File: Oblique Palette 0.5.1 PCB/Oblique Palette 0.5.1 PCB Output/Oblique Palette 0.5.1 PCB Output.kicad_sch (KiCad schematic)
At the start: 25 parts

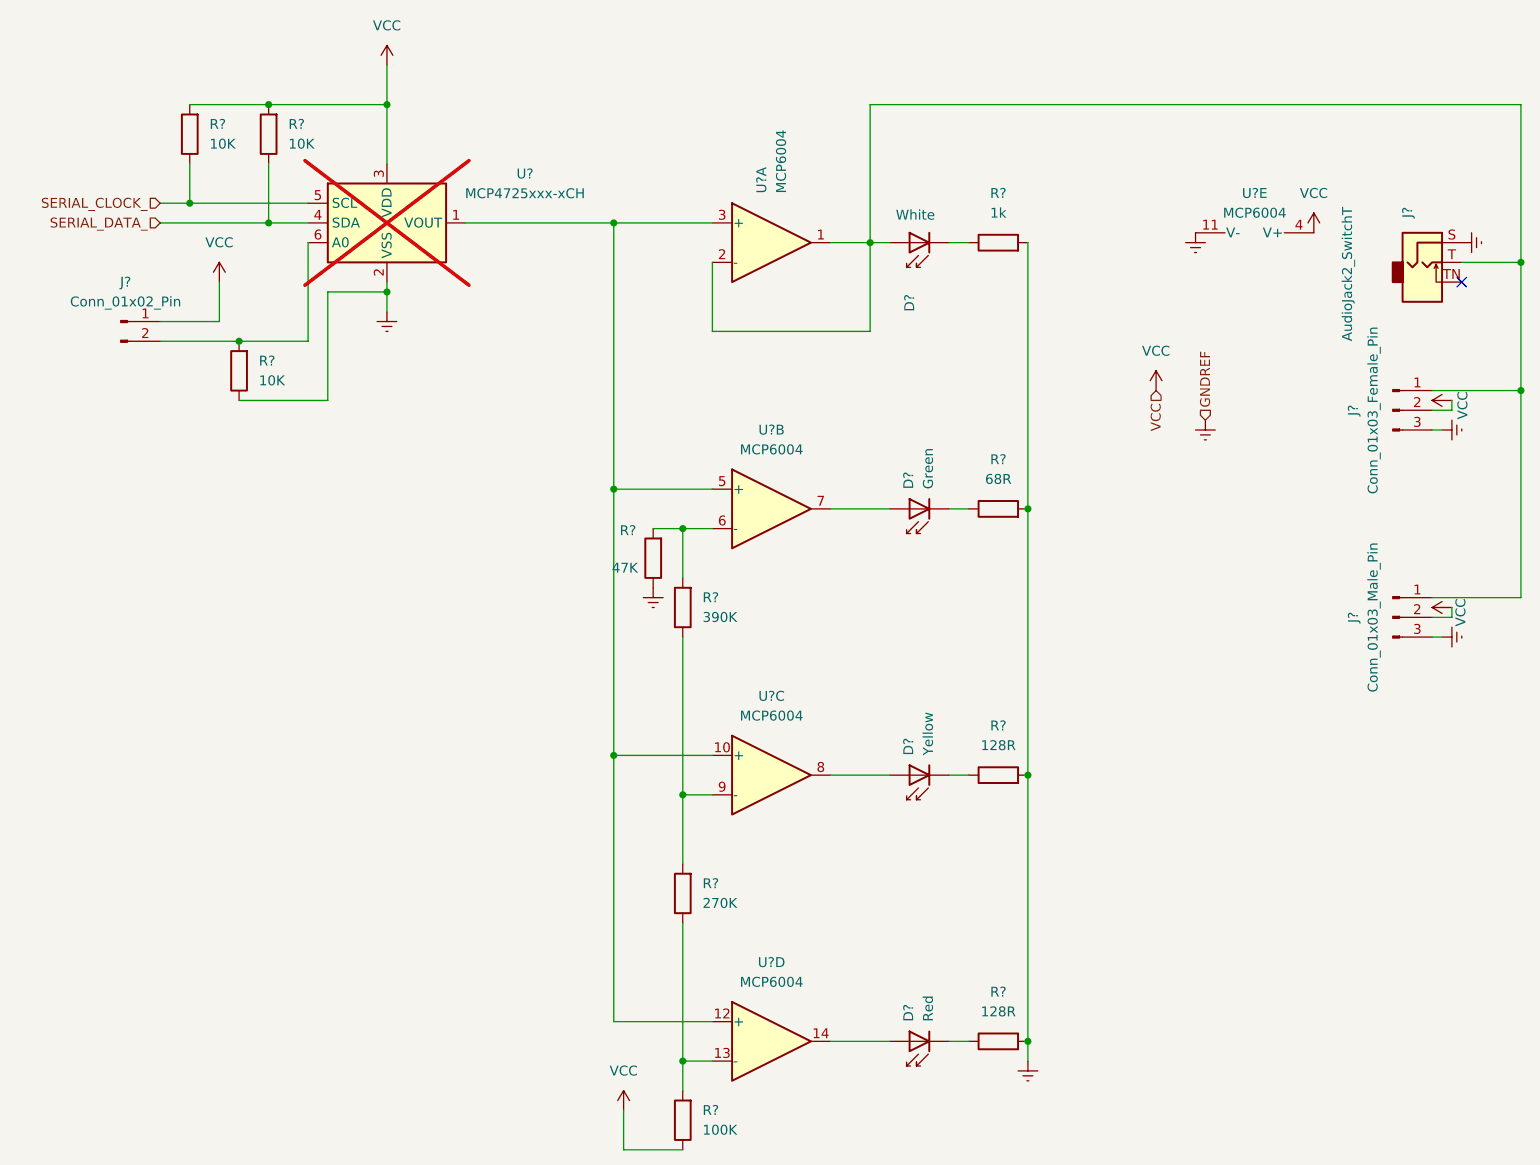
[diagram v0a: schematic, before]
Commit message: PCB corrections for 0.5.3
• Main output LED is now between op amp and feedback loop, so it will brighten at the first whiff of voltage.
• Errant wire between VBus and input potentiometer will allow us to have signals other than 5V
• Servos are now powered by V_SERVO as well as VBus.

TO DO: Differentiate A0 and A1 DACs
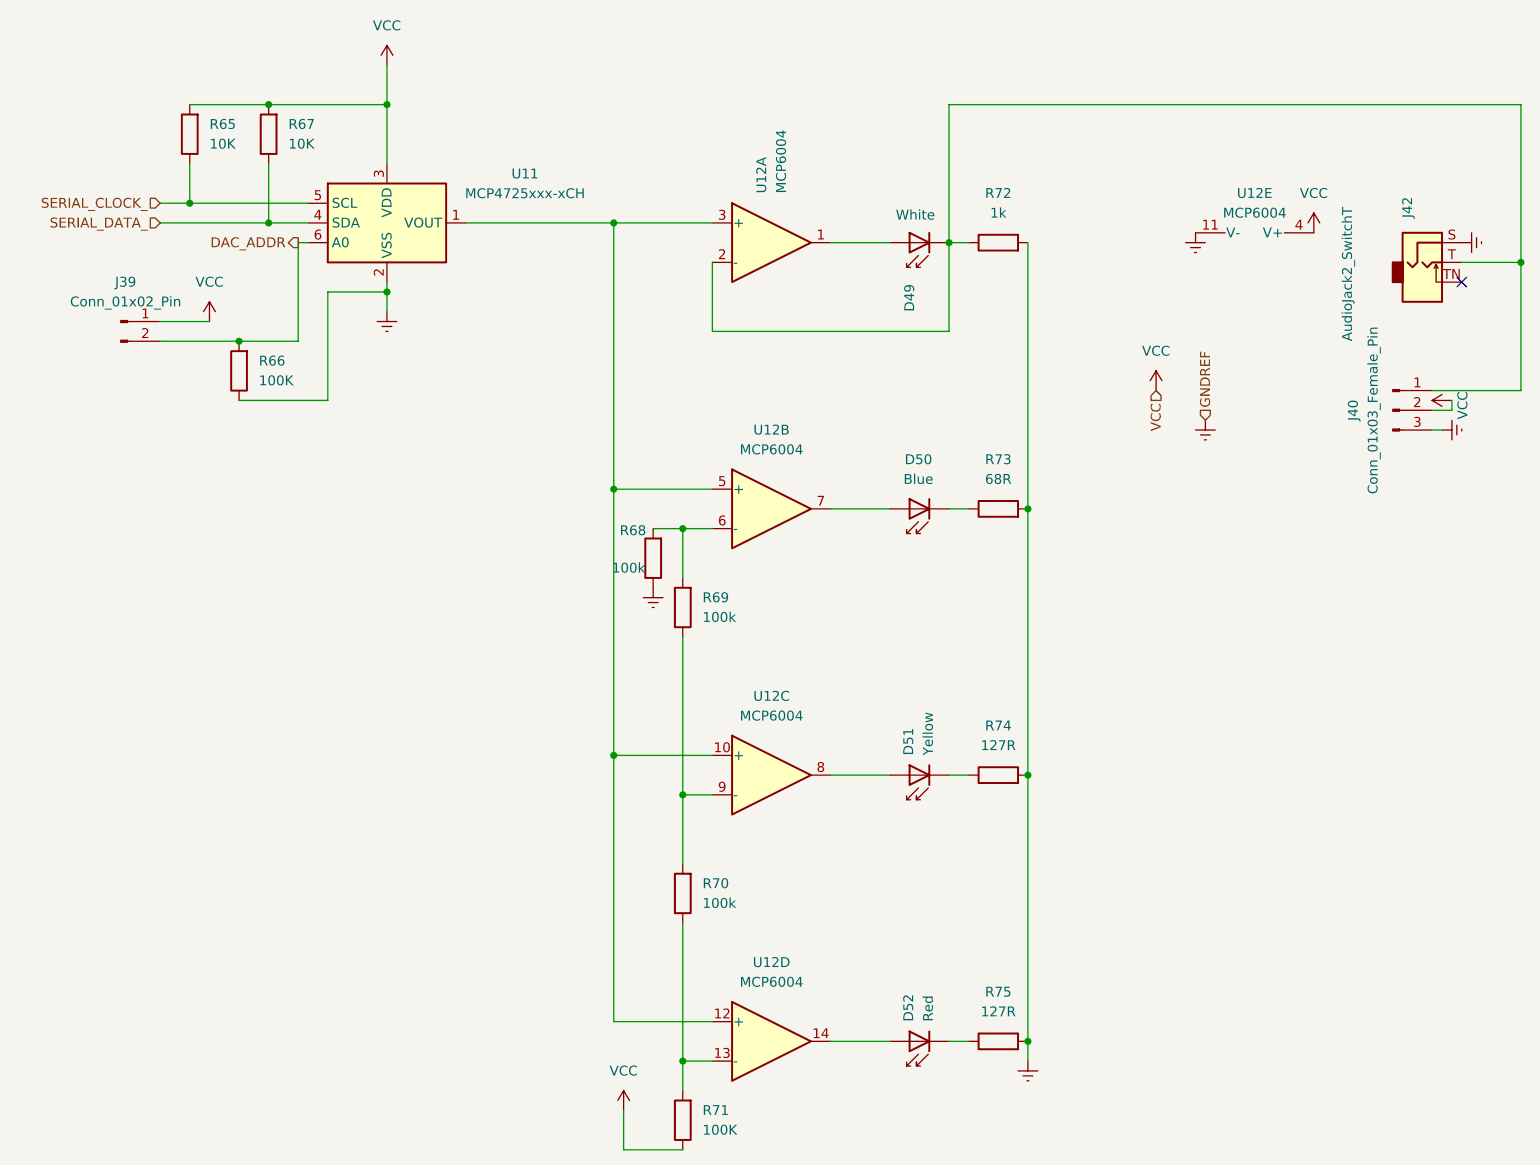
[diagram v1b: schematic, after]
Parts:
- removed J?: Conn_01x03_Male_Pin, Connector_PinHeader_2.54mm:PinHeader_1x03_P2.54mm_Vertical, symbol Connector:Conn_01x03_Pin
- D50: renamed from D?; value Green -> Blue
- R66: renamed from R?; value 10K -> 100K
- R68: renamed from R?; value 47K -> 100k
- R69: renamed from R?; value 390K -> 100k
- R70: renamed from R?; value 270K -> 100k
- R74, R75: renamed from R?; value 128R -> 127R
- U11: renamed from U?; now fitted
- gave numbers to parts that had none: 12
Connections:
- net DAC_ADDR: now reaches J39.2 (Pin_2), R66.2, U11.6 (A0)
- net at J40.1 (Pin_1), J42.T, U12.2 (-): now also D49.1 (K), R72.1; no longer D49.2 (A), U12.1
- new net: D49.2 (A), U12.1

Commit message: Update OUTPUT channels with 3 LEDs and appropriate resistors
Output channels how have RED (>3.6V), YELLOW (<2.7V) and WHITE (<0, increasing in brightness up to 5V) indicator LEDs.

Output op amp now has a 1k resistor to prevent in-use whoopsies.
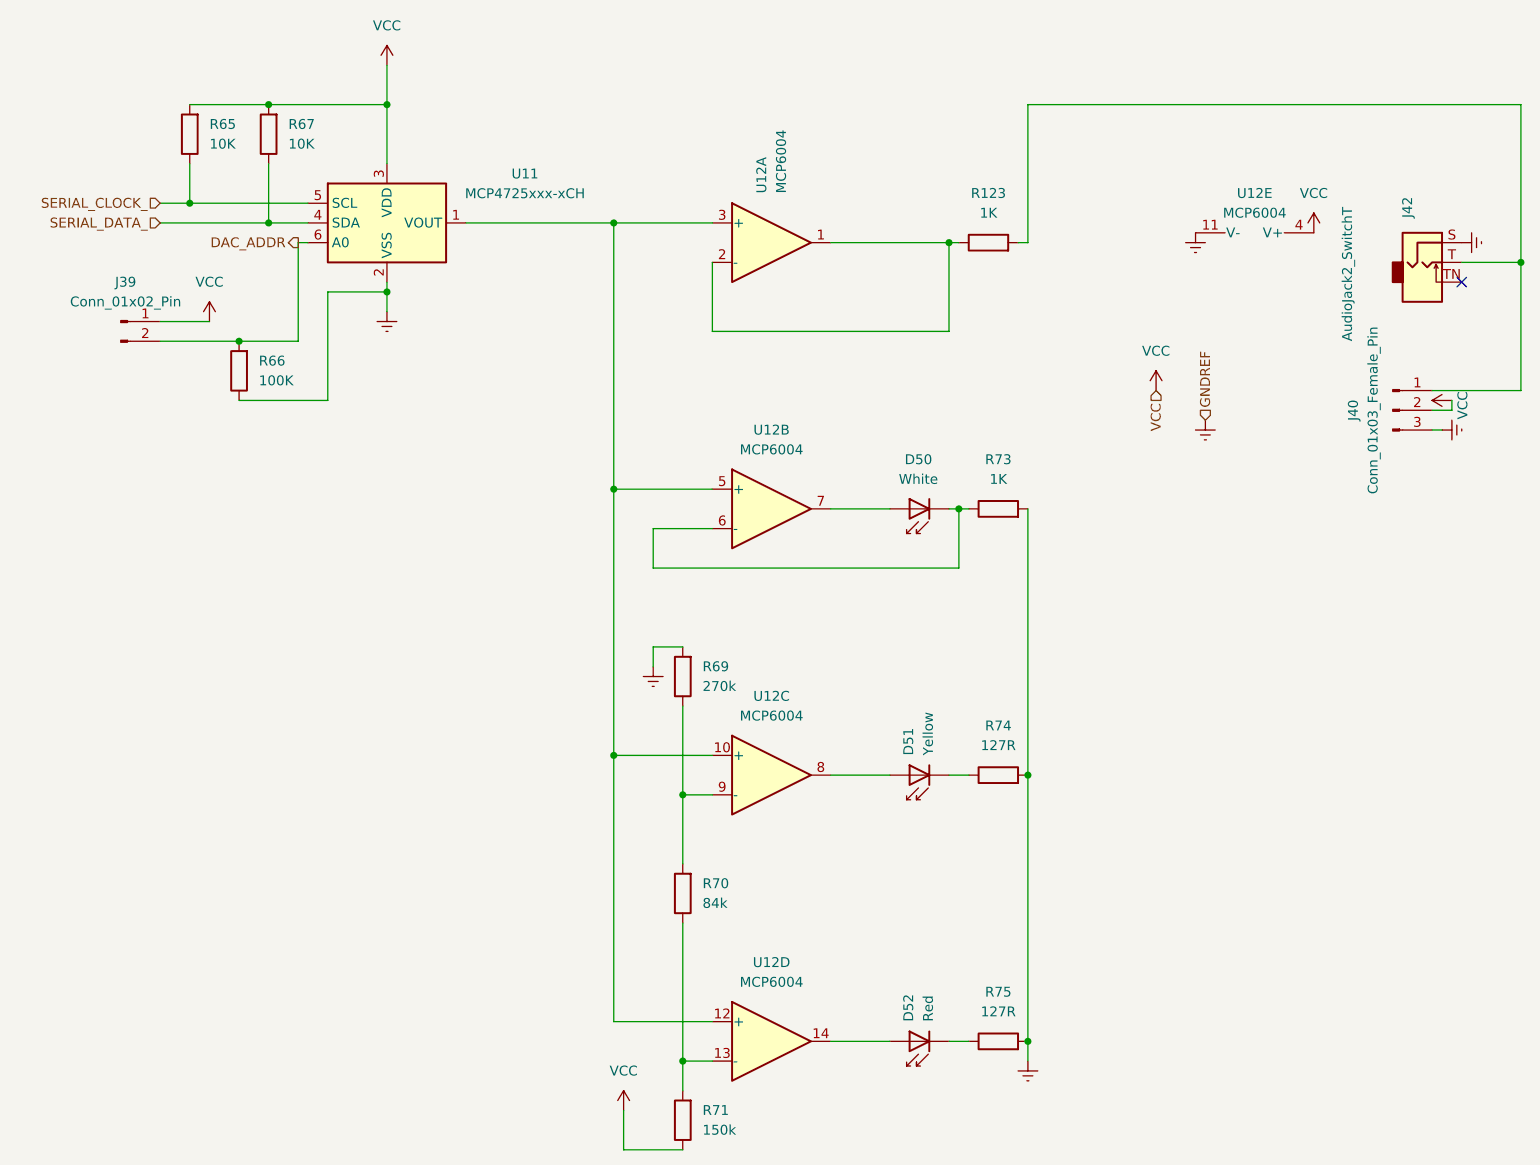
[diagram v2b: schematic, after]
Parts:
- removed D49: White, LED_THT:LED_SideEmitter_Rectangular_W4.5mm_H1.6mm, symbol LED:IRL81A
- removed R68: 100k, Resistor_SMD:R_0805_2012Metric, symbol Device:R
- removed R72: 1k, Resistor_SMD:R_0805_2012Metric, symbol Device:R
- added R123: 1K, Resistor_SMD:R_0805_2012Metric, symbol Device:R
- D50: value Blue -> White
- R69: value 100k -> 270k
- R70: value 100k -> 84k
- R71: value 100K -> 150k
- R73: value 68R -> 1K
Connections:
- net GNDREF: now also R69.2
- net at U12.6 (-): now also D50.1 (K), R73.1; no longer R69.2
- net at J40.1 (Pin_1), J42.T: now also R123.2; no longer U12.2 (-)
- net at U12.1: now also U12.2 (-), R123.1
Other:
- moved on the sheet: R69

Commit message: More input and output channel corrections
Reduced the white LED inputs to have a range of 0V:3.3V to get a greater range of brightness across the range of values

Powered the input op amps from 3v3 so we can't blow up. Changed the comparison voltage for the LEDs to 0V:3.3V instead of up to 5 so brightnesses are consistent between input and output channels.
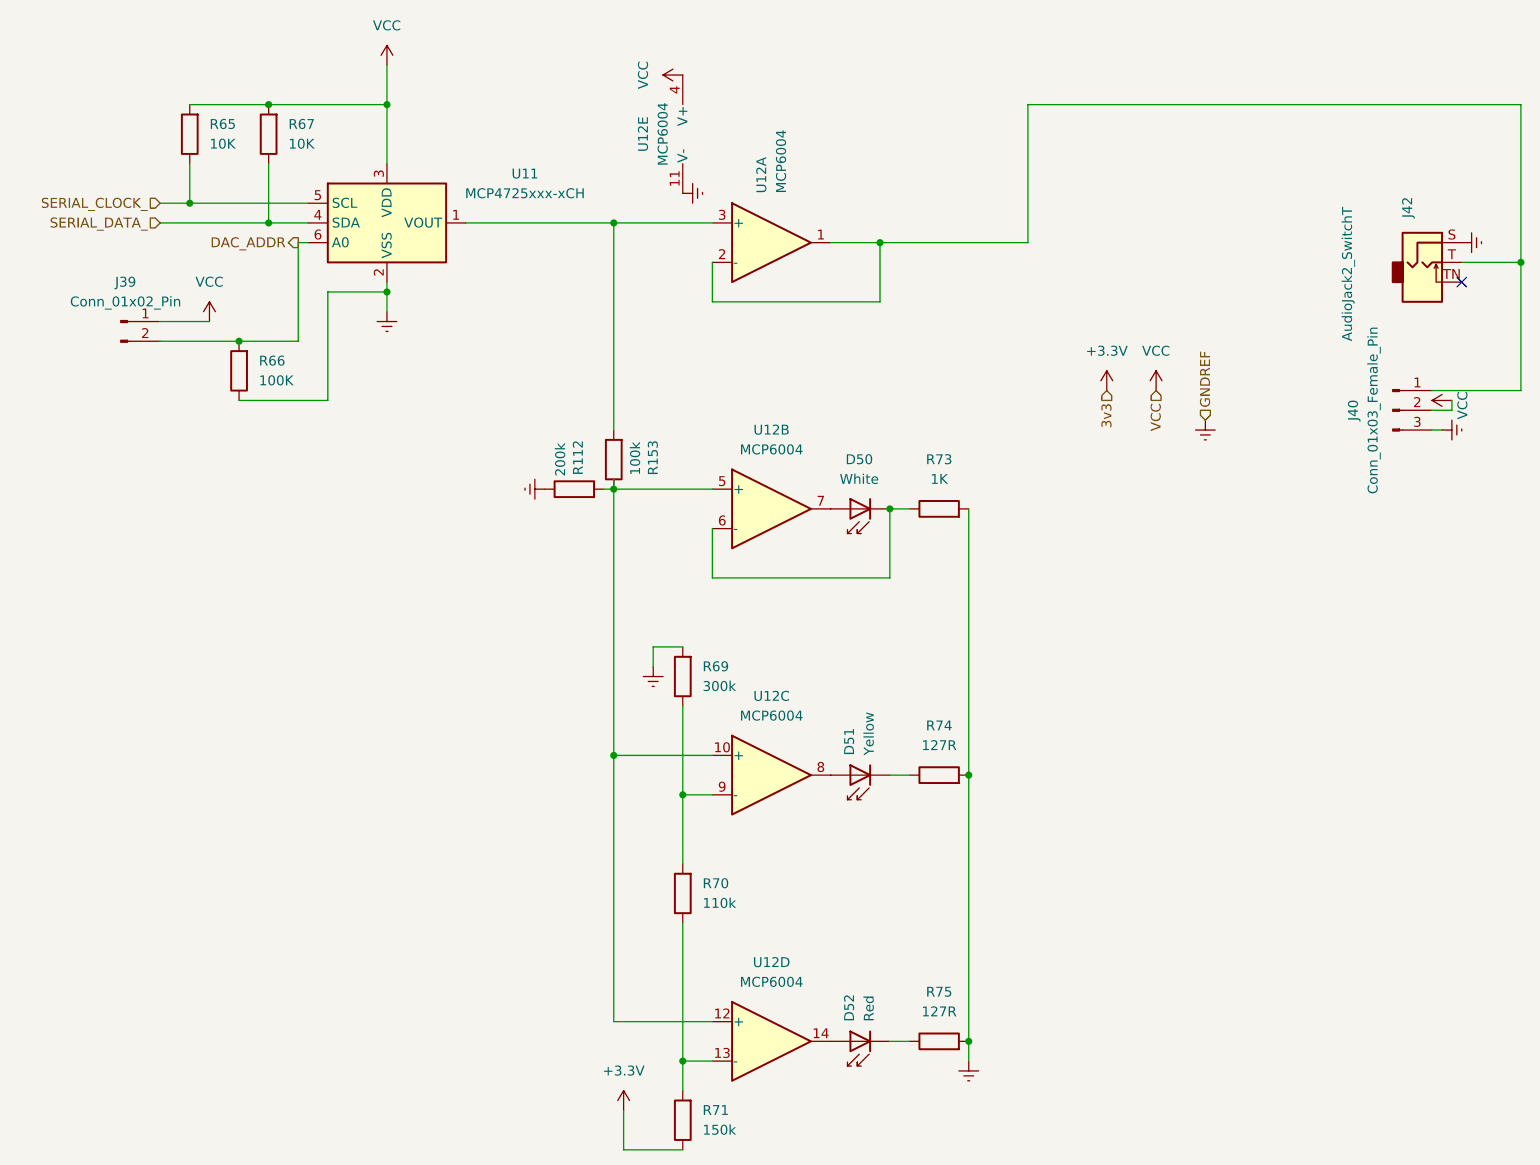
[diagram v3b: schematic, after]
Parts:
- removed R123: 1K, Resistor_SMD:R_0805_2012Metric, symbol Device:R
- added R112: 200k, Resistor_SMD:R_0805_2012Metric, symbol Device:R
- added R153: 100k, Resistor_SMD:R_0805_2012Metric, symbol Device:R
- R69: value 270k -> 300k
- R70: value 84k -> 110k
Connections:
- net GNDREF: now also R112.1
- net VCC: no longer R71.1
- net at U12.10 (+), U12.12 (+), U12.5 (+): now also R112.2, R153.1; no longer U11.1 (VOUT), U12.3 (+)
- net at J40.1 (Pin_1), J42.T: now also U12.1, U12.2 (-)
- new net: R153.2, U11.1 (VOUT), U12.3 (+)
- new net +3.3V: R71.1
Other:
- moved on the sheet: D50, D51, D52, R73, R74, R75, U12E

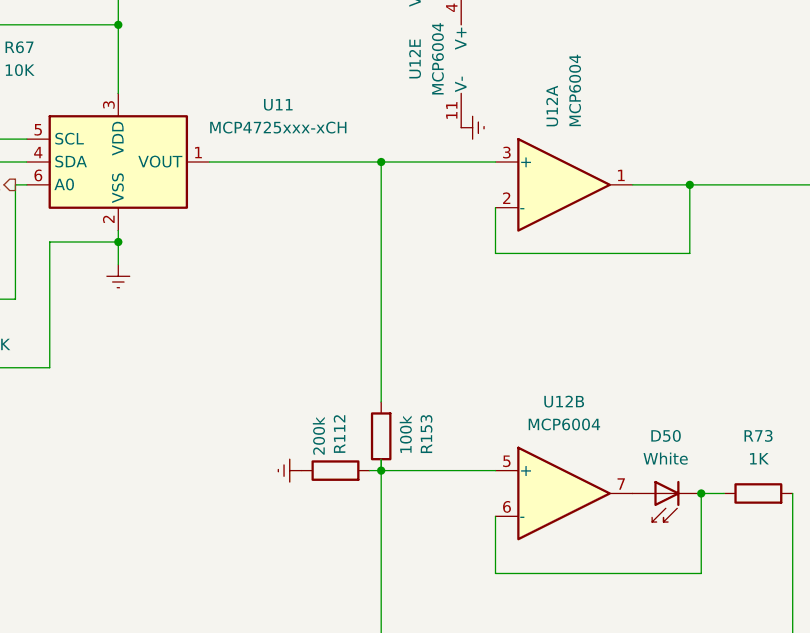
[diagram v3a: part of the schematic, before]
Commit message: Front panel channel labels
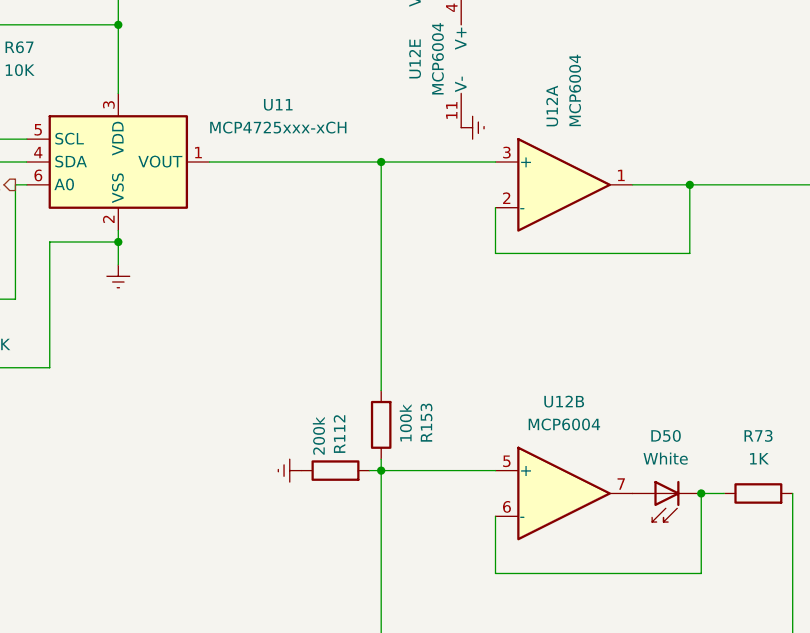
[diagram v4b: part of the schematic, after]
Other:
- moved on the sheet: R153
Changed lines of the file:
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@@
 	(wire
 		(pts
+			(xy 102.87 77.47) (xy 102.87 78.74)
+		)
+		(stroke
+			(width 0)
+			(type default)
+		)
+	)
+	(wire
+		(pts
 			(xy 58.42 36.83) (xy 58.42 44.45)
 		)
@@
 	(wire
 		(pts
-			(xy 102.87 77.47) (xy 102.87 78.74)
-		)
-		(stroke
-			(width 0)
-			(type default)
-		)
-	)
-	(wire
-		(pts
 			(xy 73.66 29.21) (xy 73.66 36.83)
 		)
@@
 	(wire
 		(pts
-			(xy 102.87 71.12) (xy 102.87 44.45)
+			(xy 102.87 69.85) (xy 102.87 44.45)
 		)
 		(stroke
@@
 	(symbol
 		(lib_id "Device:R")
-		(at 102.87 74.93 180)
+		(at 102.87 73.66 180)
 		(unit 1)
 		(exclude_from_sim no)
@@
 		(dnp no)
 		(property "Reference" "R153"
-			(at 107.95 76.9621 90)
+			(at 107.95 75.6921 90)
 			(effects
 				(font
@@
 		)
 		(property "Value" "100k"
-			(at 105.664 76.962 90)
+			(at 105.664 75.692 90)
 			(effects
 				(font
@@
 		)
 		(property "Footprint" "Resistor_SMD:R_0805_2012Metric"
-			(at 104.648 74.93 90)
+			(at 104.648 73.66 90)
 			(effects
 				(font
@@
 		)
 		(property "Datasheet" "~"
-			(at 102.87 74.93 0)
+			(at 102.87 73.66 0)
 			(effects
 				(font
@@
 		)
 		(property "Description" "Resistor"
-			(at 102.87 74.93 0)
+			(at 102.87 73.66 0)
 			(effects
 				(font
